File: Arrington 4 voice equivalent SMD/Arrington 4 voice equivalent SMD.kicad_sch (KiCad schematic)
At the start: 19 parts, among them J1 SJ1-3525N, J2 DB25_Male, J3 RCJ-013, SW1 SW_SPDT, U1 74LS05, U2 74LS05

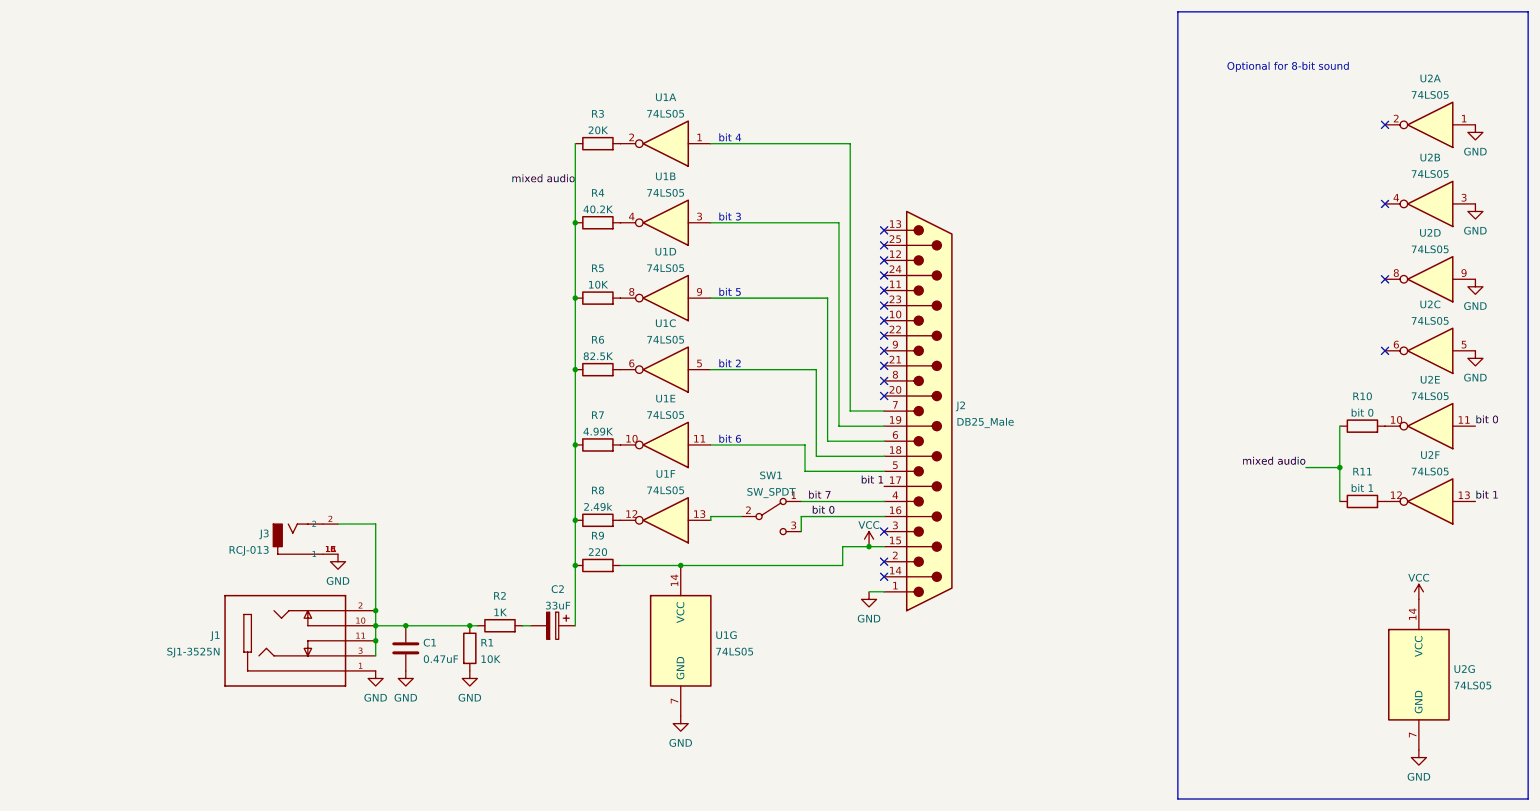
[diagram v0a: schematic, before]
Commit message: removed outdated gerbers, updated design to version 2
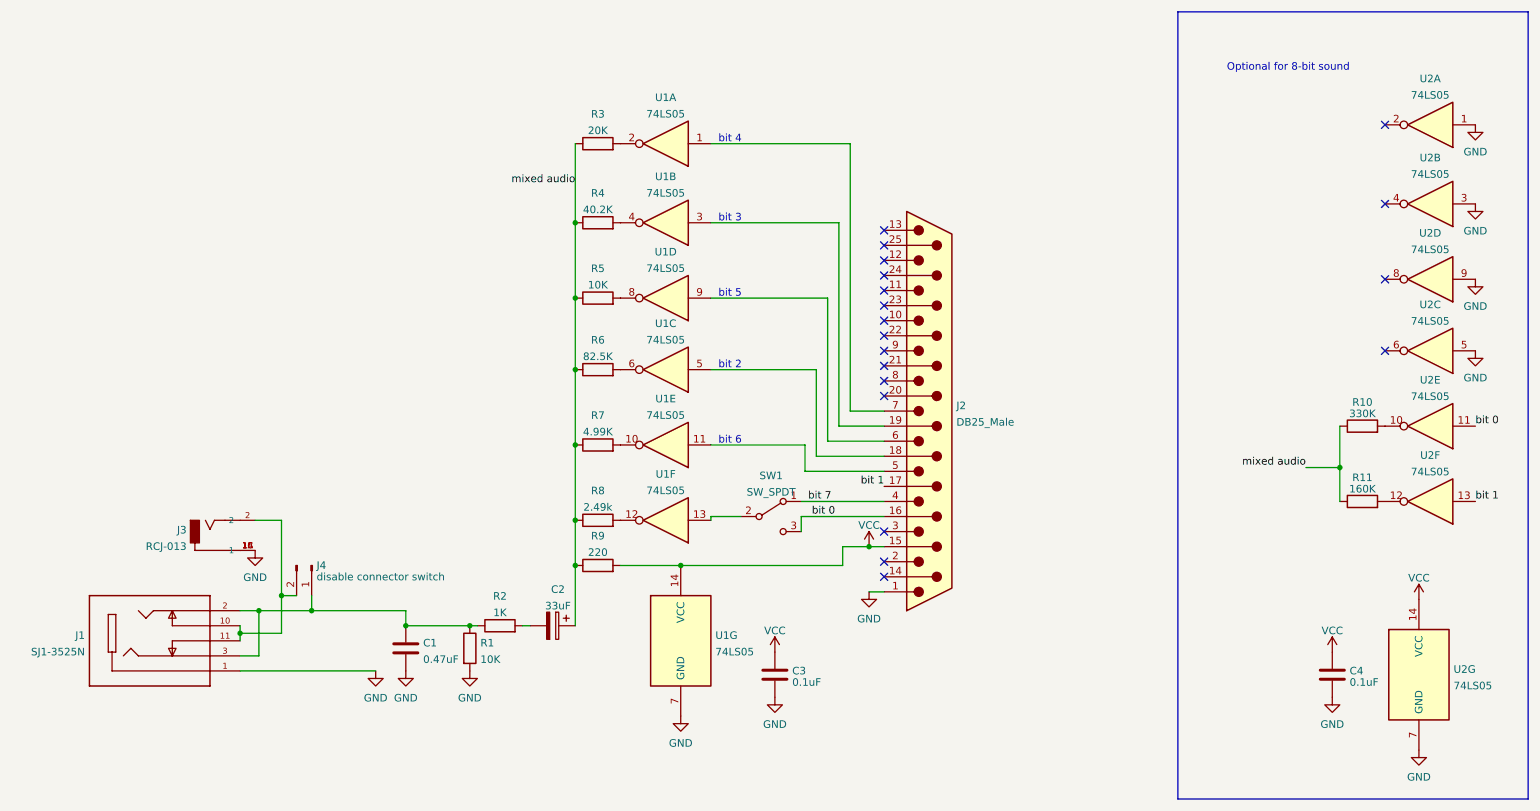
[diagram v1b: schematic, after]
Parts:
- added C3, C4: 0.1uF, Capacitor_SMD:C_0603_1608Metric, symbol Device:C
- added J4: disable connector switch, Connector_PinHeader_2.54mm:PinHeader_1x02_P2.54mm_Vertical, symbol Connector:Conn_01x02_Pin
- R10: value bit 0 -> 330K
- R11: value bit 1 -> 160K
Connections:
- net GND: now also C3.2, C4.2
- net VCC: now also C3.1, C4.1
- net at C1.1, J1.2, J1.3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: now also J4.1 (Pin_1); no longer J1.10, J1.11, J3.2
- new net: J1.10, J1.11, J3.2, J4.2 (Pin_2)
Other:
- moved on the sheet: J1, J3
